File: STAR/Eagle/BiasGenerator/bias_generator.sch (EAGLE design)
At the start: 21 parts, among them T1 750311838, U1 LT8300, U2 LT8330

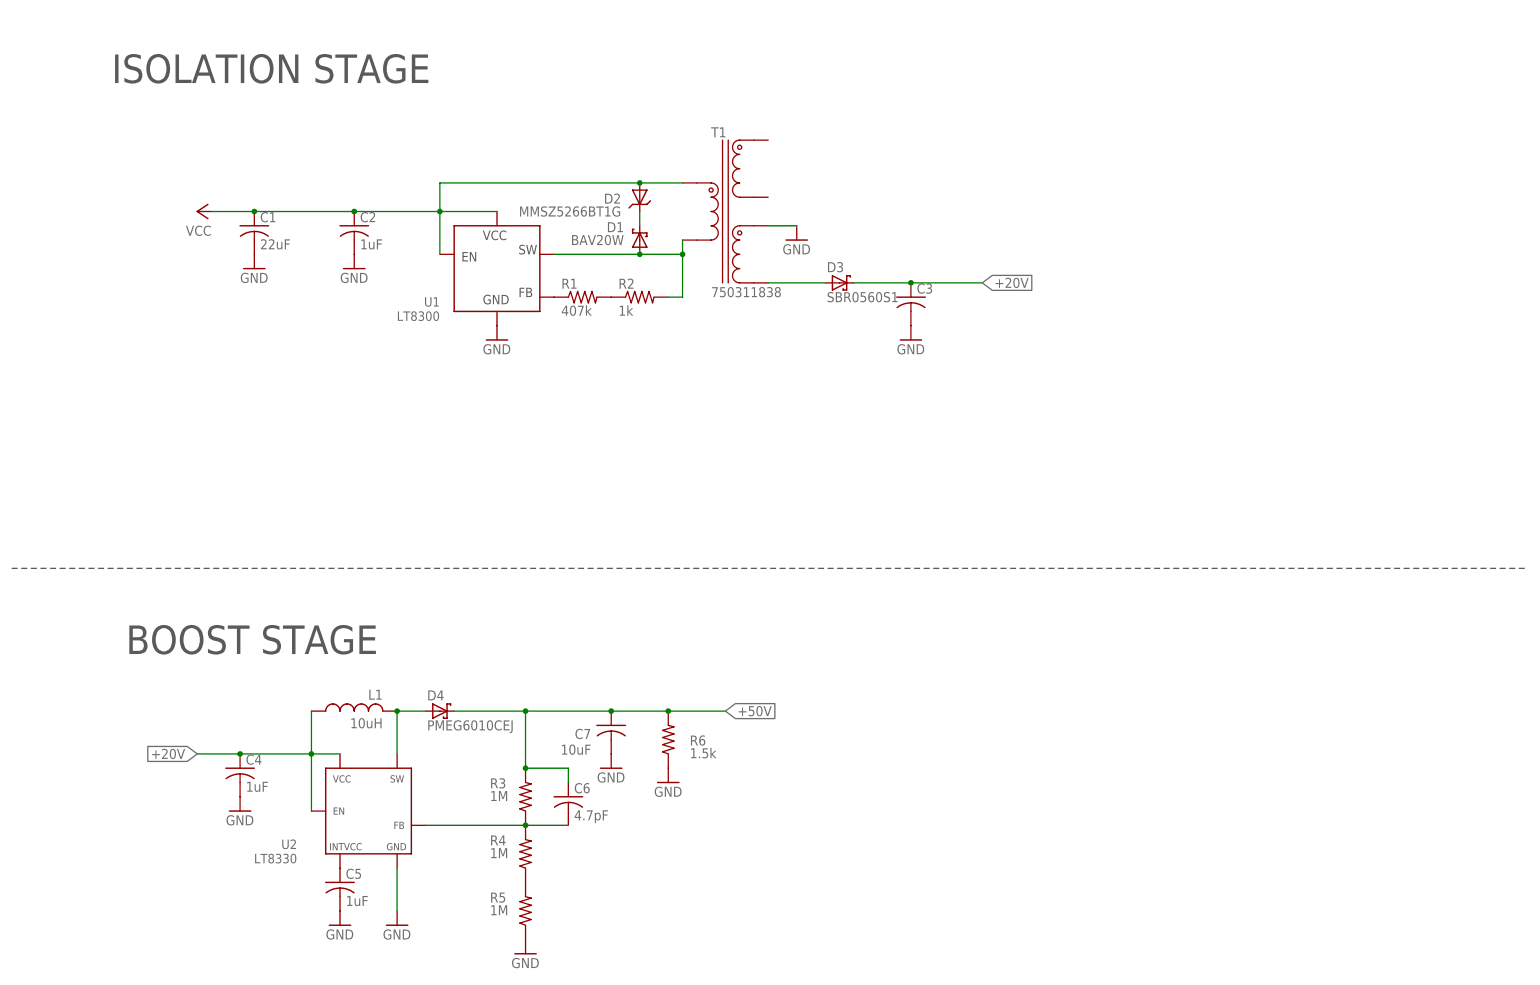
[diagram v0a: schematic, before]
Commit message: fixed datalogger USB port
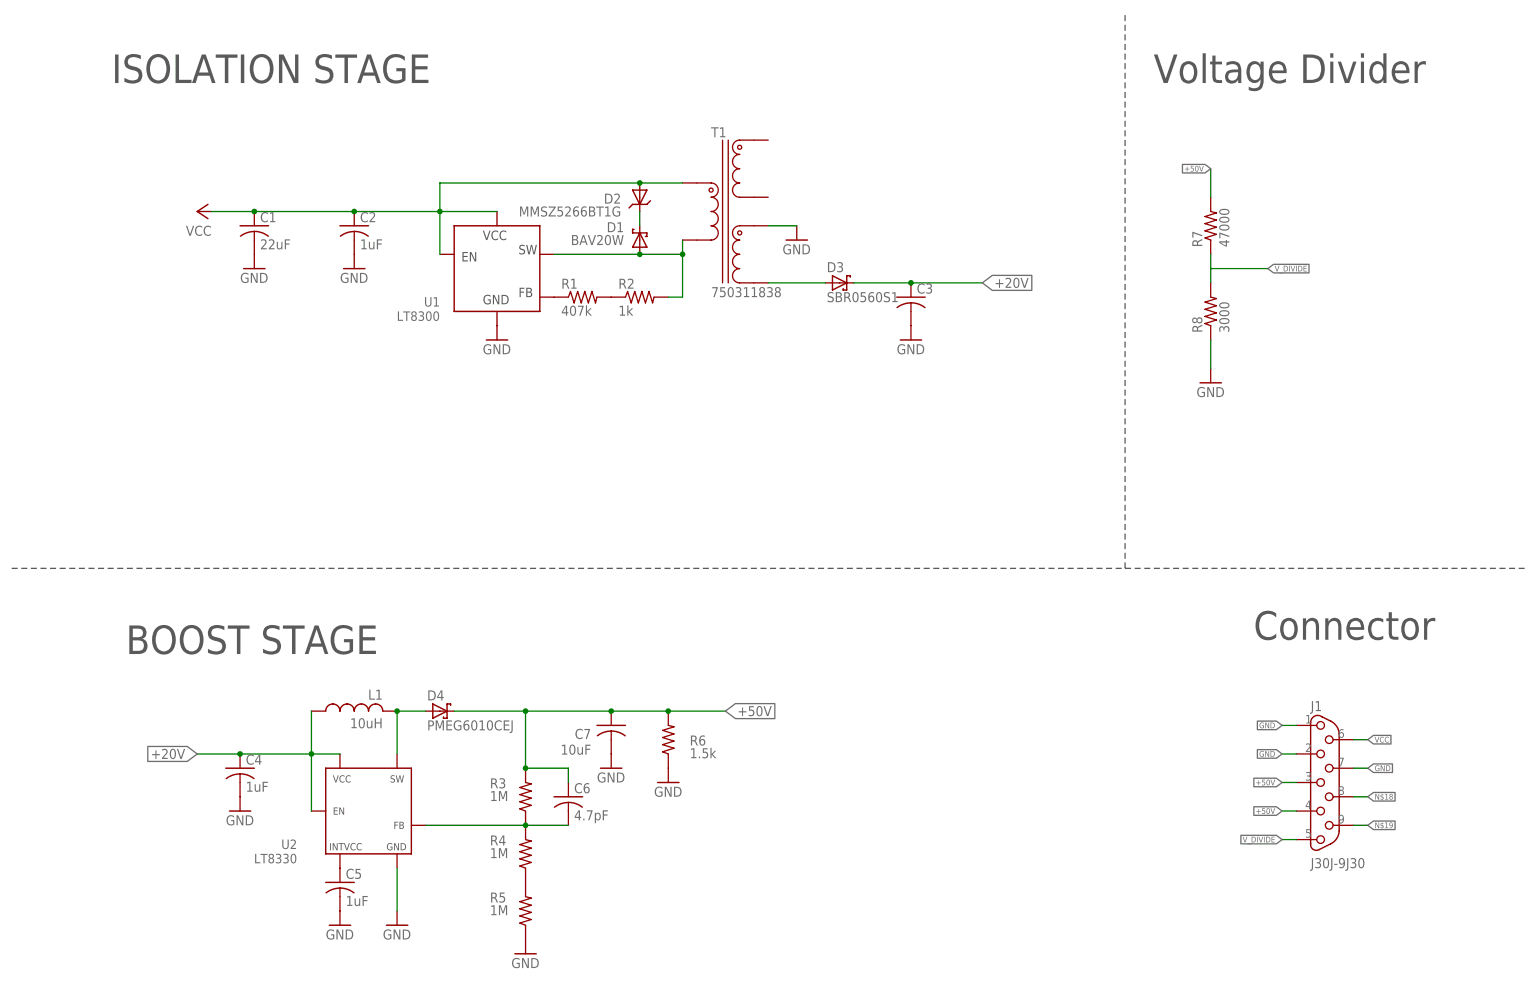
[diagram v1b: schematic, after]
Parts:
- added J1: J30J-9J30, CM_J30J:J30J-9J30
- added R7: 47000, resistor:R-US_R0603
- added R8: 3000, resistor:R-US_R0603
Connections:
- new net N$18: J1.8
- new net N$19: J1.9
- new net V_DIVIDE: J1.5, R7.1, R8.2
- net +50V: now also J1.3, J1.4, R7.2
- net GND: now also J1.1, J1.2, J1.7, R8.1
- net VCC: now also J1.6
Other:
- note added: "Connector"
- note added: "Voltage Divider"
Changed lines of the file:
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@@
 <part name="R6" library="resistor" deviceset="R-US_" device="R2512" value="1.5k"/>
 <part name="GND11" library="supply1" deviceset="GND" device=""/>
+<part name="R7" library="resistor" deviceset="R-US_" device="R0603" value="47000"/>
+<part name="R8" library="resistor" deviceset="R-US_" device="R0603" value="3000"/>
+<part name="GND12" library="supply1" deviceset="GND" device=""/>
+<part name="J1" library="CM_J30J" deviceset="J30J-9" device="J30"/>
 </parts>
 <sheets>
 <sheet>
 <plain>
-<wire x1="5.08" y1="111.76" x2="274.32" y2="111.76" width="0.1524" layer="97" style="shortdash"/>
+<wire x1="5.08" y1="111.76" x2="203.2" y2="111.76" width="0.1524" layer="97" style="shortdash"/>
 <text x="22.86" y="198.12" size="5.08" layer="97">ISOLATION STAGE</text>
 <text x="25.4" y="96.52" size="5.08" layer="97">BOOST STAGE</text>
+<text x="208.28" y="198.12" size="5.08" layer="97">Voltage Divider</text>
+<wire x1="203.2" y1="111.76" x2="274.32" y2="111.76" width="0.1524" layer="97" style="shortdash"/>
+<wire x1="203.2" y1="111.76" x2="203.2" y2="210.82" width="0.1524" layer="97" style="shortdash"/>
+<text x="226.06" y="99.06" size="5.08" layer="97">Connector</text>
 </plain>
 <instances>
@@
 </instance>
 <instance part="GND11" gate="1" x="121.92" y="73.66"/>
+<instance part="R7" gate="G$1" x="218.44" y="172.72" rot="R90"/>
+<instance part="R8" gate="G$1" x="218.44" y="157.48" rot="R90"/>
+<instance part="GND12" gate="1" x="218.44" y="144.78"/>
+<instance part="J1" gate="G$1" x="238.76" y="73.66"/>
 </instances>
 <busses>
@@
 <junction x="48.26" y="175.26"/>
 </segment>
+<segment>
+<pinref part="J1" gate="G$1" pin="6"/>
+<wire x1="243.84" y1="81.28" x2="246.38" y2="81.28" width="0.1524" layer="91"/>
+<label x="246.38" y="81.28" size="1.016" layer="95" xref="yes"/>
+</segment>
 </net>
 <net name="GND" class="0">
@@
 <pinref part="R6" gate="G$1" pin="1"/>
 <pinref part="GND11" gate="1" pin="GND"/>
+</segment>
+<segment>
+<pinref part="R8" gate="G$1" pin="1"/>
+<wire x1="218.44" y1="152.4" x2="218.44" y2="147.32" width="0.1524" layer="91"/>
+<pinref part="GND12" gate="1" pin="GND"/>
+</segment>
+<segment>
+<pinref part="J1" gate="G$1" pin="1"/>
+<wire x1="233.68" y1="83.82" x2="231.14" y2="83.82" width="0.1524" layer="91"/>
+<label x="231.14" y="83.82" size="1.016" layer="95" rot="R180" xref="yes"/>
+</segment>
+<segment>
+<pinref part="J1" gate="G$1" pin="2"/>
+<wire x1="233.68" y1="78.74" x2="231.14" y2="78.74" width="0.1524" layer="91"/>
+<label x="231.14" y="78.74" size="1.016" layer="95" rot="R180" xref="yes"/>
+</segment>
+<segment>
+<pinref part="J1" gate="G$1" pin="7"/>
+<wire x1="243.84" y1="76.2" x2="246.38" y2="76.2" width="0.1524" layer="91"/>
+<label x="246.38" y="76.2" size="1.016" layer="95" xref="yes"/>
 </segment>
 </net>
@@
 <label x="132.08" y="86.36" size="1.778" layer="95" xref="yes"/>
 </segment>
+<segment>
+<pinref part="R7" gate="G$1" pin="2"/>
+<wire x1="218.44" y1="177.8" x2="218.44" y2="182.88" width="0.1524" layer="91"/>
+<label x="218.44" y="182.88" size="1.016" layer="95" rot="R180" xref="yes"/>
+</segment>
+<segment>
+<pinref part="J1" gate="G$1" pin="3"/>
+<wire x1="233.68" y1="73.66" x2="231.14" y2="73.66" width="0.1524" layer="91"/>
+<label x="231.14" y="73.66" size="1.016" layer="95" rot="R180" xref="yes"/>
+</segment>
+<segment>
+<pinref part="J1" gate="G$1" pin="4"/>
+<wire x1="233.68" y1="68.58" x2="231.14" y2="68.58" width="0.1524" layer="91"/>
+<label x="231.14" y="68.58" size="1.016" layer="95" rot="R180" xref="yes"/>
+</segment>
 </net>
 <net name="N$11" class="0">
@@
 </segment>
 </net>
+<net name="V_DIVIDE" class="0">
+<segment>
+<pinref part="R8" gate="G$1" pin="2"/>
+<wire x1="218.44" y1="162.56" x2="218.44" y2="165.1" width="0.1524" layer="91"/>
+<wire x1="218.44" y1="165.1" x2="228.6" y2="165.1" width="0.1524" layer="91"/>
+<pinref part="R7" gate="G$1" pin="1"/>
+<wire x1="218.44" y1="165.1" x2="218.44" y2="167.64" width="0.1524" layer="91"/>
+<label x="228.6" y="165.1" size="1.016" layer="95" xref="yes"/>
+</segment>
+<segment>
+<pinref part="J1" gate="G$1" pin="5"/>
+<wire x1="233.68" y1="63.5" x2="231.14" y2="63.5" width="0.1524" layer="91"/>
+<label x="231.14" y="63.5" size="1.016" layer="95" rot="R180" xref="yes"/>
+</segment>
+</net>
+<net name="N$18" class="0">
+<segment>
+<pinref part="J1" gate="G$1" pin="8"/>
+<wire x1="243.84" y1="71.12" x2="246.38" y2="71.12" width="0.1524" layer="91"/>
+<label x="246.38" y="71.12" size="1.016" layer="95" xref="yes"/>
+</segment>
+</net>
+<net name="N$19" class="0">
+<segment>
+<pinref part="J1" gate="G$1" pin="9"/>
+<wire x1="243.84" y1="66.04" x2="246.38" y2="66.04" width="0.1524" layer="91"/>
+<label x="246.38" y="66.04" size="1.016" layer="95" xref="yes"/>
+</segment>
+</net>

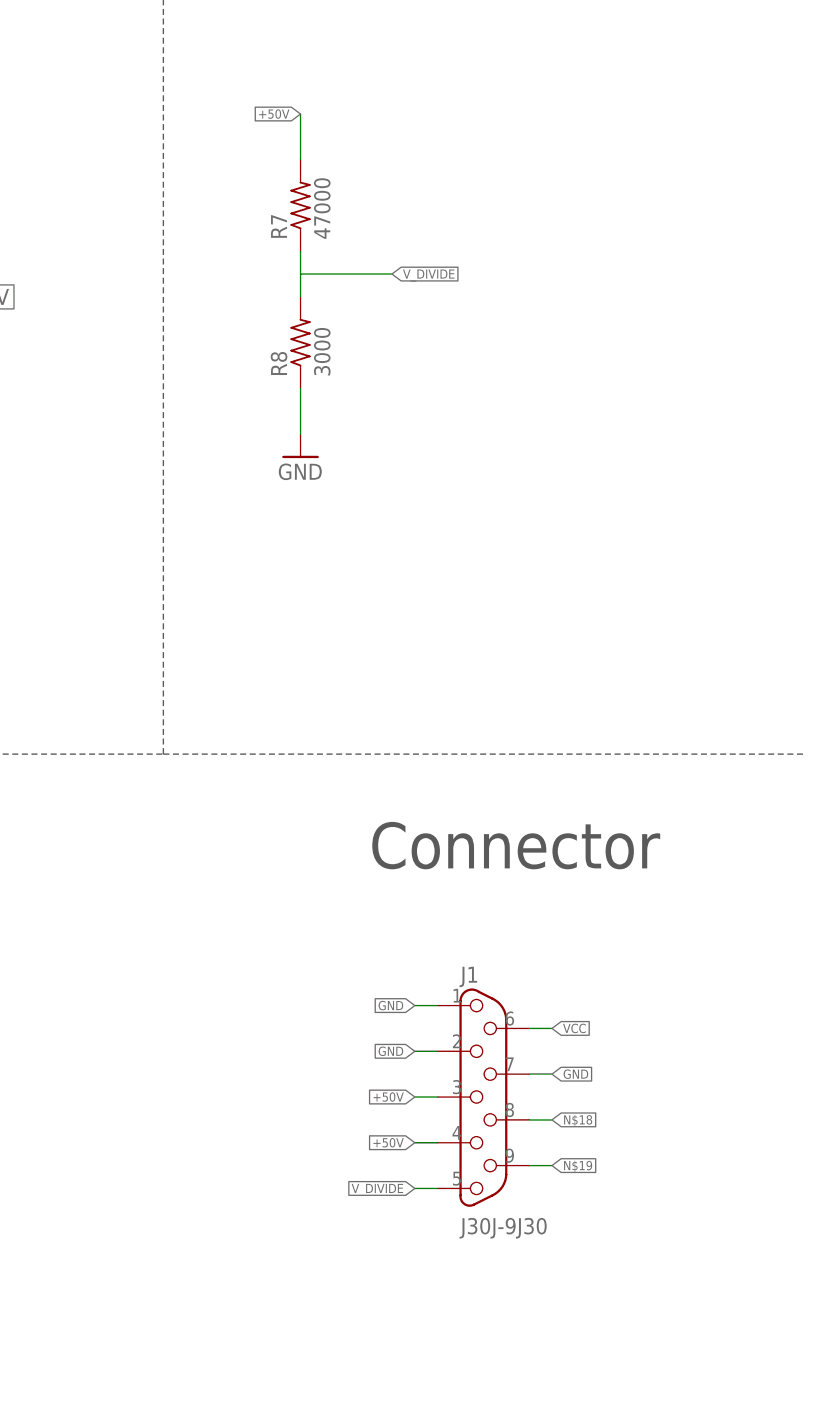
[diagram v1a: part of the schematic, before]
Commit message: M2 drills
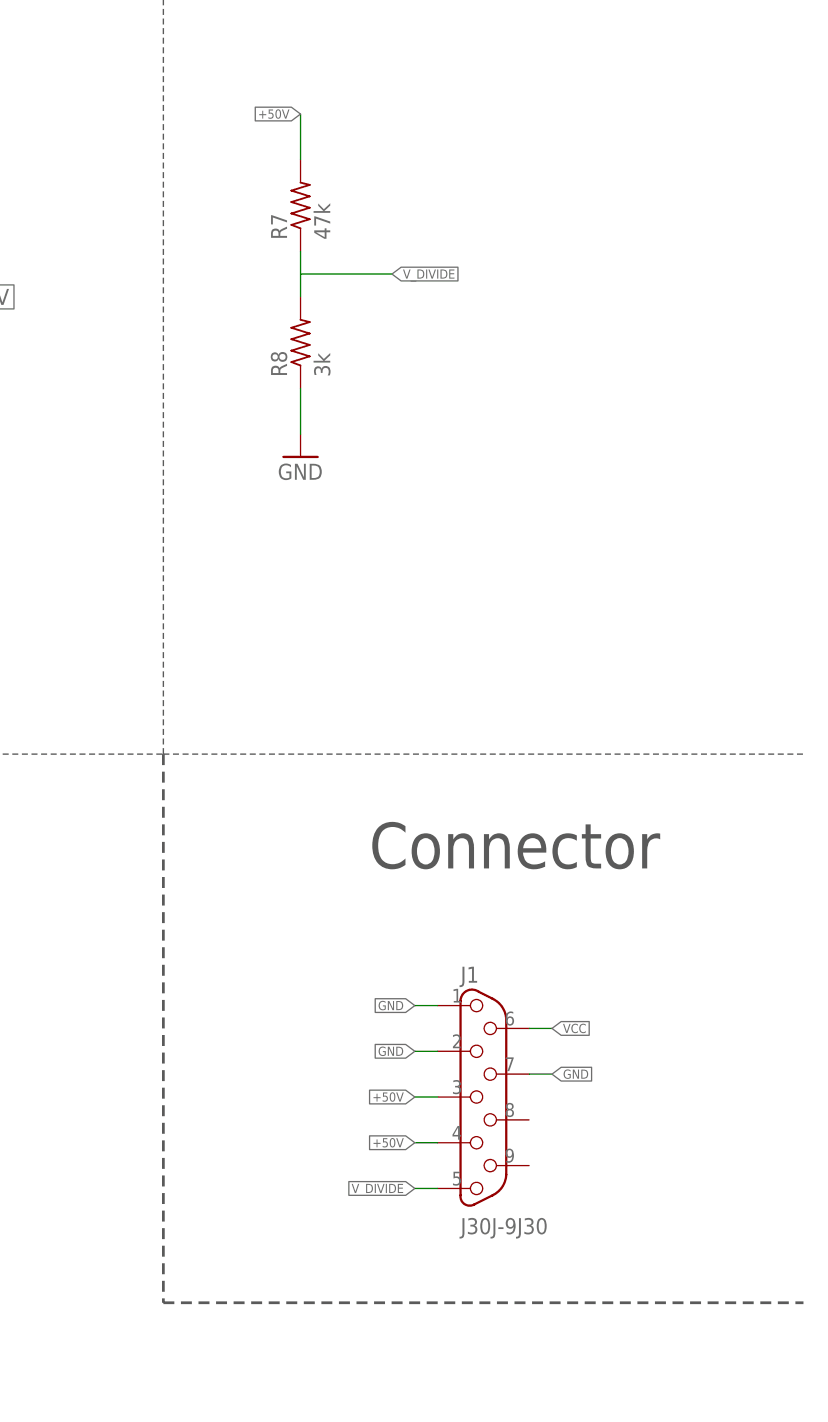
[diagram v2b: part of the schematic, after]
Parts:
- R7: value 47000 -> 47k; device resistor:R-US_R0603 -> resistor:R-US_R2512
- R8: value 3000 -> 3k; device resistor:R-US_R0603 -> resistor:R-US_R2512
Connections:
- removed net N$18: J1.8
- removed net N$19: J1.9
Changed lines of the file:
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@@
 <part name="R6" library="resistor" deviceset="R-US_" device="R2512" value="1.5k"/>
 <part name="GND11" library="supply1" deviceset="GND" device=""/>
-<part name="R7" library="resistor" deviceset="R-US_" device="R0603" value="47000"/>
-<part name="R8" library="resistor" deviceset="R-US_" device="R0603" value="3000"/>
 <part name="GND12" library="supply1" deviceset="GND" device=""/>
 <part name="J1" library="CM_J30J" deviceset="J30J-9" device="J30"/>
+<part name="R7" library="resistor" deviceset="R-US_" device="R2512" value="47k"/>
+<part name="R8" library="resistor" deviceset="R-US_" device="R2512" value="3k"/>
 </parts>
 <sheets>
@@
 <wire x1="203.2" y1="111.76" x2="203.2" y2="210.82" width="0.1524" layer="97" style="shortdash"/>
 <text x="226.06" y="99.06" size="5.08" layer="97">Connector</text>
+<wire x1="203.2" y1="111.76" x2="203.2" y2="50.8" width="0.3048" layer="97" style="shortdash"/>
+<wire x1="203.2" y1="50.8" x2="274.32" y2="50.8" width="0.3048" layer="97" style="shortdash"/>
 </plain>
 <instances>
@@
 </instance>
 <instance part="GND11" gate="1" x="121.92" y="73.66"/>
+<instance part="GND12" gate="1" x="218.44" y="144.78"/>
+<instance part="J1" gate="G$1" x="238.76" y="73.66"/>
 <instance part="R7" gate="G$1" x="218.44" y="172.72" rot="R90"/>
 <instance part="R8" gate="G$1" x="218.44" y="157.48" rot="R90"/>
-<instance part="GND12" gate="1" x="218.44" y="144.78"/>
-<instance part="J1" gate="G$1" x="238.76" y="73.66"/>
 </instances>
 <busses>
@@
 </segment>
 <segment>
-<pinref part="R8" gate="G$1" pin="1"/>
 <wire x1="218.44" y1="152.4" x2="218.44" y2="147.32" width="0.1524" layer="91"/>
 <pinref part="GND12" gate="1" pin="GND"/>
+<pinref part="R8" gate="G$1" pin="1"/>
 </segment>
 <segment>
@@
 </segment>
 <segment>
-<pinref part="R7" gate="G$1" pin="2"/>
 <wire x1="218.44" y1="177.8" x2="218.44" y2="182.88" width="0.1524" layer="91"/>
 <label x="218.44" y="182.88" size="1.016" layer="95" rot="R180" xref="yes"/>
+<pinref part="R7" gate="G$1" pin="2"/>
 </segment>
 <segment>
@@
 <net name="V_DIVIDE" class="0">
 <segment>
-<pinref part="R8" gate="G$1" pin="2"/>
 <wire x1="218.44" y1="162.56" x2="218.44" y2="165.1" width="0.1524" layer="91"/>
 <wire x1="218.44" y1="165.1" x2="228.6" y2="165.1" width="0.1524" layer="91"/>
-<pinref part="R7" gate="G$1" pin="1"/>
 <wire x1="218.44" y1="165.1" x2="218.44" y2="167.64" width="0.1524" layer="91"/>
 <label x="228.6" y="165.1" size="1.016" layer="95" xref="yes"/>
+<pinref part="R7" gate="G$1" pin="1"/>
+<pinref part="R8" gate="G$1" pin="2"/>
 </segment>
 <segment>
@@
 </segment>
 </net>
-<net name="N$18" class="0">
-<segment>
-<pinref part="J1" gate="G$1" pin="8"/>
-<wire x1="243.84" y1="71.12" x2="246.38" y2="71.12" width="0.1524" layer="91"/>
-<label x="246.38" y="71.12" size="1.016" layer="95" xref="yes"/>
-</segment>
-</net>
-<net name="N$19" class="0">
-<segment>
-<pinref part="J1" gate="G$1" pin="9"/>
-<wire x1="243.84" y1="66.04" x2="246.38" y2="66.04" width="0.1524" layer="91"/>
-<label x="246.38" y="66.04" size="1.016" layer="95" xref="yes"/>
-</segment>
-</net>
